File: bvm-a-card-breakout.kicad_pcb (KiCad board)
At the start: 4 copper layers, 37.2 x 76.1 mm, 6 parts, among them J1 mezz-conn-02x50, J2 mezz-conn-02x50, J3 Conn_01x25, J4 Conn_01x25, J5 Conn_01x25, J6 Conn_01x25

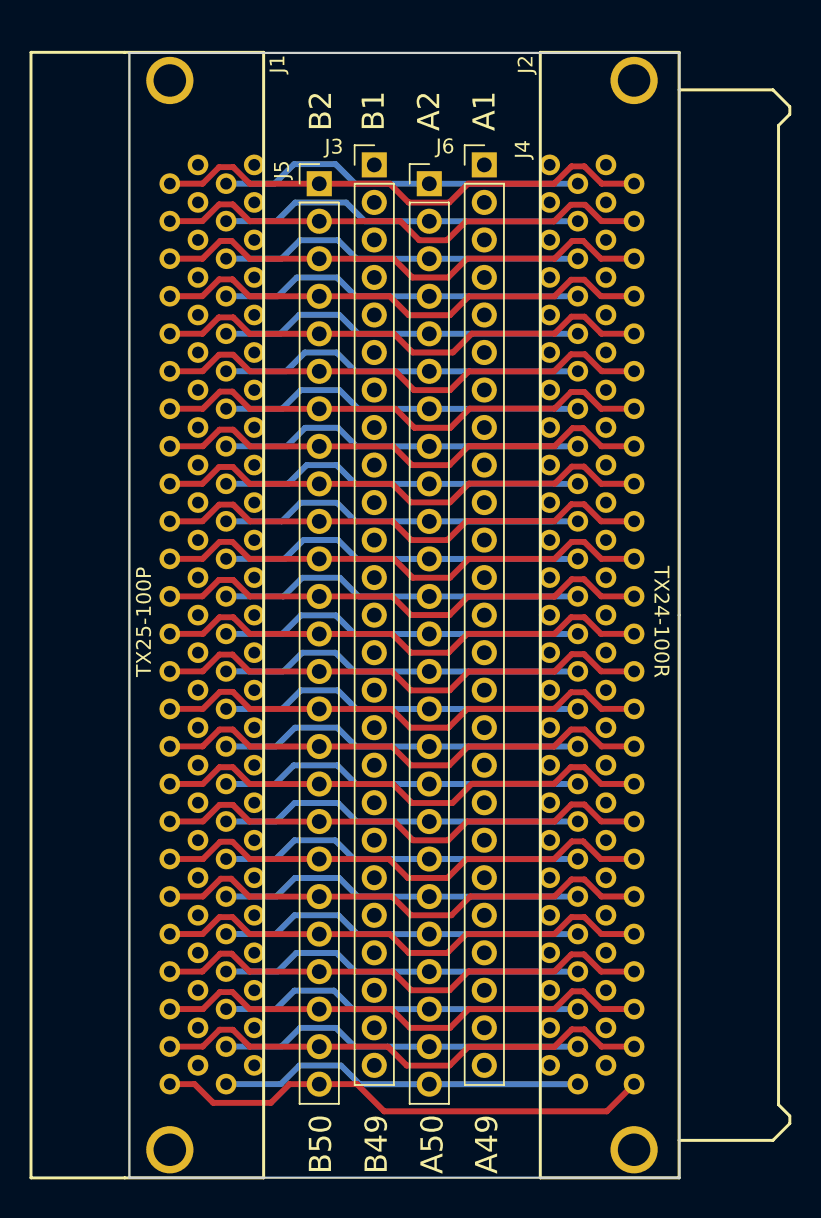
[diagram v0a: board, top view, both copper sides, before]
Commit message: Fixed slight misalignment in connector footprints
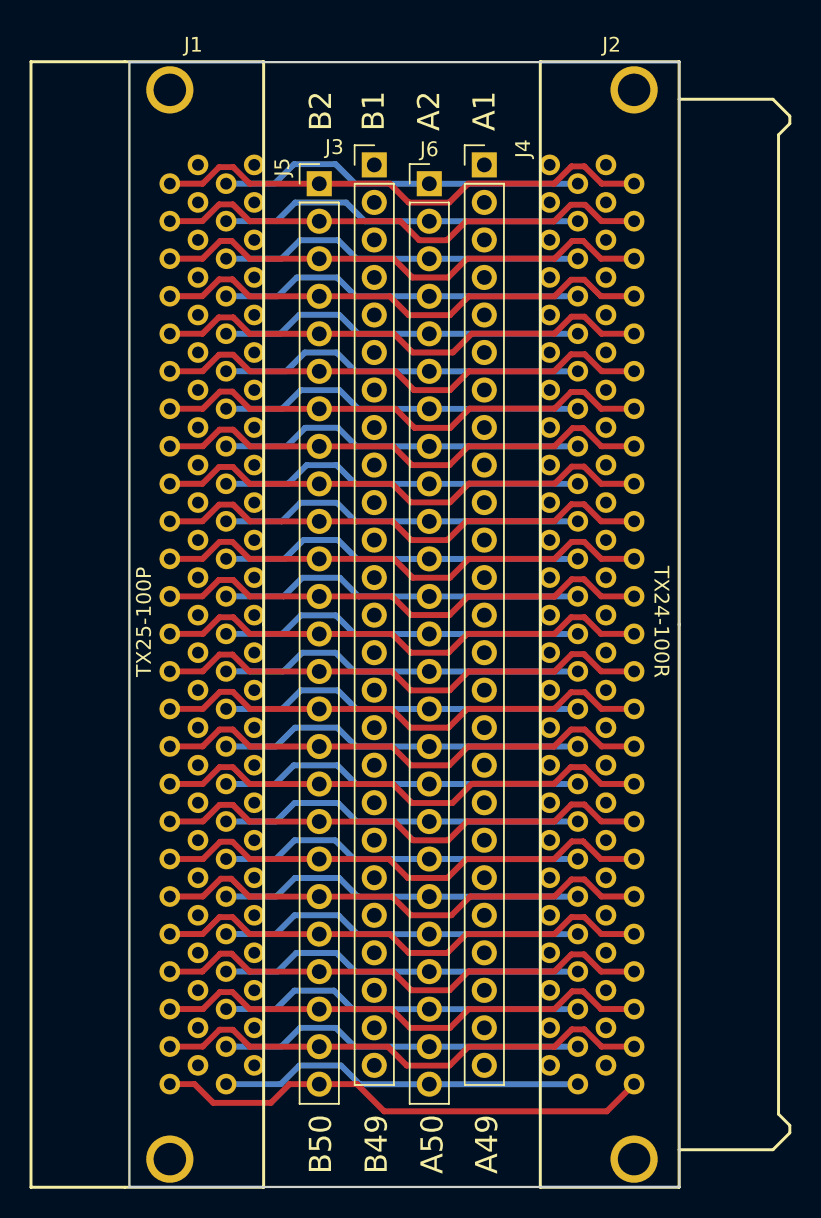
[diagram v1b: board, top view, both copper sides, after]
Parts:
- J1: footprint TX25-100P-LT-H1E:TX24-100R-LT-H1E -> TX25-100P-LT-H1E:TX25-100P-LT-H1E

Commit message: Updated to full-size Z-board replacement
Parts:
- added H1: Keystone 7794, keystone-7794:7794-X, F.Cu at (129.8, 301.4)
- added H2: Keystone 7794, keystone-7794:7794-X, F.Cu at (129.8, 79.5)
- added J11: mezz-conn-02x50, TX25-100P-LT-H1E:TX25-100P-LT-H1E, F.Cu at (130.4, 223.2)
- added J12: mezz-conn-02x50, TX24-100R-LT-H1E:TX24-100R-LT-H1E, F.Cu at (339.9, 223.2)
- added J13: Conn_01x25, Connector_PinHeader_2.54mm:PinHeader_1x25_P2.54mm_Vertical, F.Cu at (138.5, 223.2)
- added J14: Conn_01x25, Connector_PinHeader_2.54mm:PinHeader_1x25_P2.54mm_Vertical, F.Cu at (145.9, 223.2)
- added J15: Conn_01x25, Connector_PinHeader_2.54mm:PinHeader_1x25_P2.54mm_Vertical, F.Cu at (134.8, 224.4)
- added J16: Conn_01x25, Connector_PinHeader_2.54mm:PinHeader_1x25_P2.54mm_Vertical, F.Cu at (142.2, 224.4)
- J3, J4, J5, J6: footprint Pin_Headers:Pin_Header_Straight_1x25_Pitch2.54mm -> Connector_PinHeader_2.54mm:PinHeader_1x25_P2.54mm_Vertical
- moved J2 155.4 mm to (339.9, 95.4)
- moved J1 46.0 mm to (130.4, 95.4)
- moved J4 46.0 mm to (145.9, 95.4)
- moved J5 46.0 mm to (134.8, 96.6)
- moved J6 46.0 mm to (142.2, 96.6)
- moved J3 46.0 mm to (138.5, 95.4)
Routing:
- net B1_2: track 0.00 -> 232.4 mm
- net B16_2: track 0.00 -> 224.5 mm
- net B6_2: track 0.00 -> 224.5 mm
- net B40_2: track 0.00 -> 224.5 mm
- net B44_2: track 0.00 -> 224.5 mm
- net B46_2: track 0.00 -> 224.5 mm
- net B38_2: track 0.00 -> 224.5 mm
- net B34_2: track 0.00 -> 224.5 mm
- net B32_2: track 0.00 -> 224.4 mm
- net B14_2: track 0.00 -> 224.4 mm
- net B28_2: track 0.00 -> 224.4 mm
- net B48_2: track 0.00 -> 224.4 mm
- net B42_2: track 0.00 -> 224.4 mm
- net B18_2: track 0.00 -> 224.4 mm
- net B30_2: track 0.00 -> 224.4 mm
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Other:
- board size 37.2 x 76.1 mm -> 230.4 x 233.5 mm
- rule pad_to_mask_clearance: 0.2 -> 0
- board text added: "(2022) Martin Hejnfelt, martin@hejnfelt.com www.immerhax.com"
- board text added: "3 5 7 9 11 13 15 17 19 21 23 25 27 29 31 33 35 37 39 41 43 45 47"
- board text added: "4 6 8 10 12 14 16 18 20 22 24 26 28 30 32 34 36 38 40 42 44 46 48"
- board text added: "BVM-A Card Breakout"
- board text added: "Rev. A"
